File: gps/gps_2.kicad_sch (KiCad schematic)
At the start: 43 parts, among them J1 Programming Header, J2 G125-MH104M4-04AD000P, J3 SMA_CONN, U1 M10578-A2, U2 PIC18F26K83, U3 MCP2562, U4 SPX3819M5-L-3-3, U5 INA180

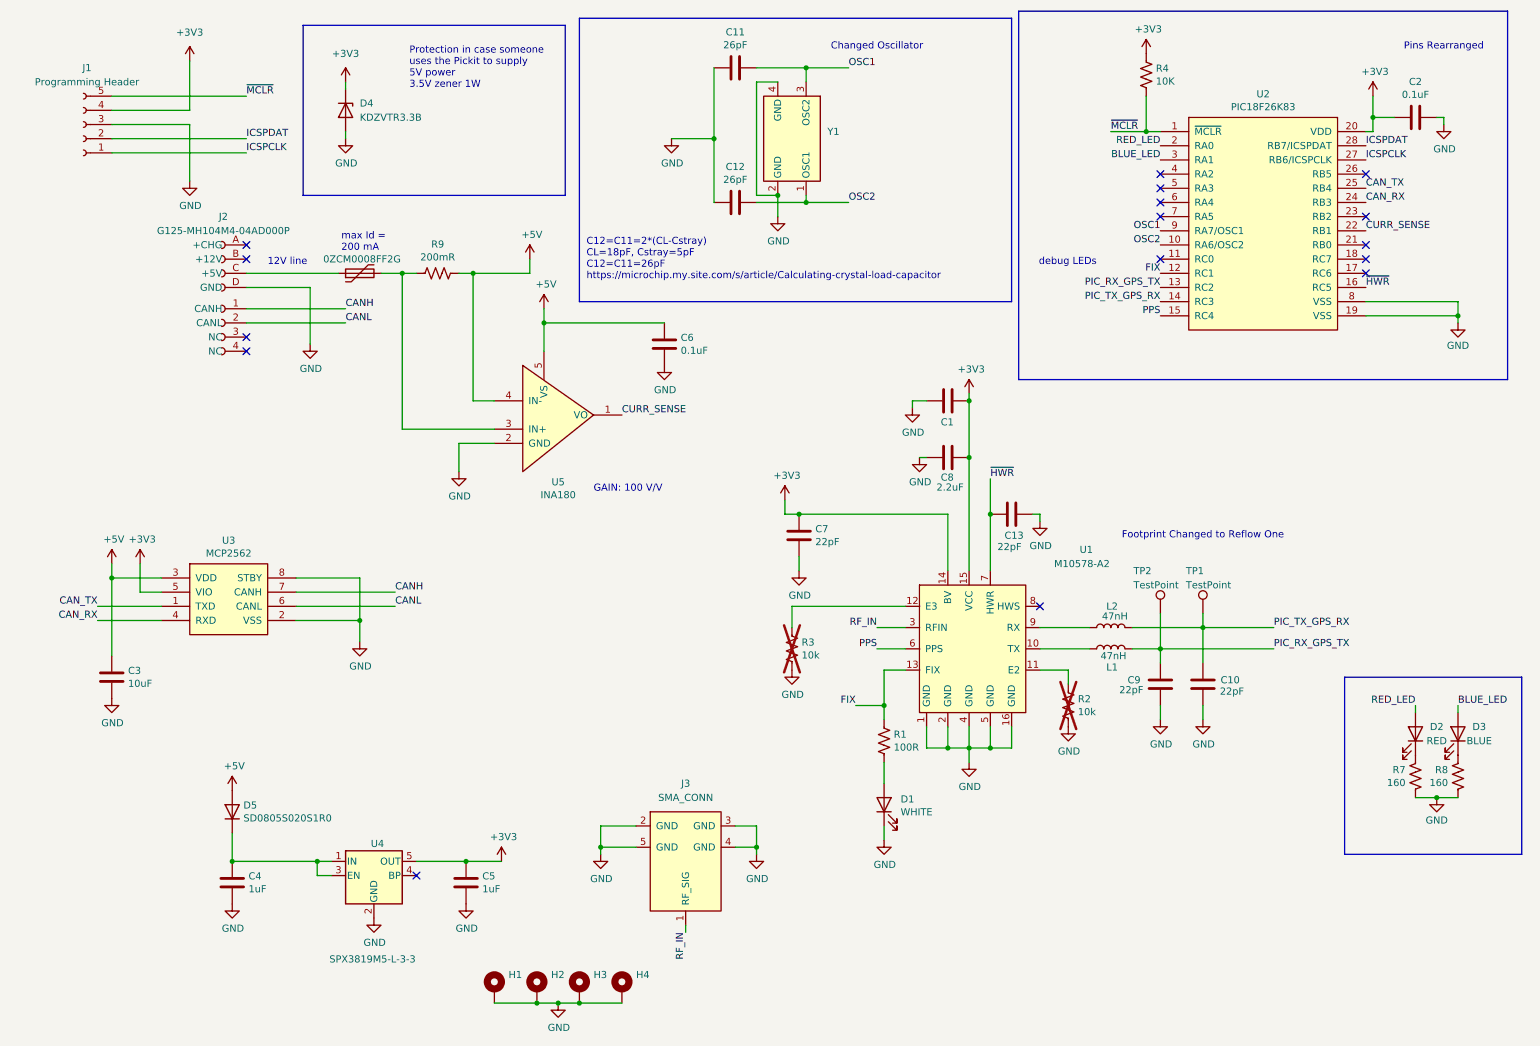
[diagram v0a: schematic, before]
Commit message: Added Rio's changes except TP's for CAN. Eliminated Diode from LDO input
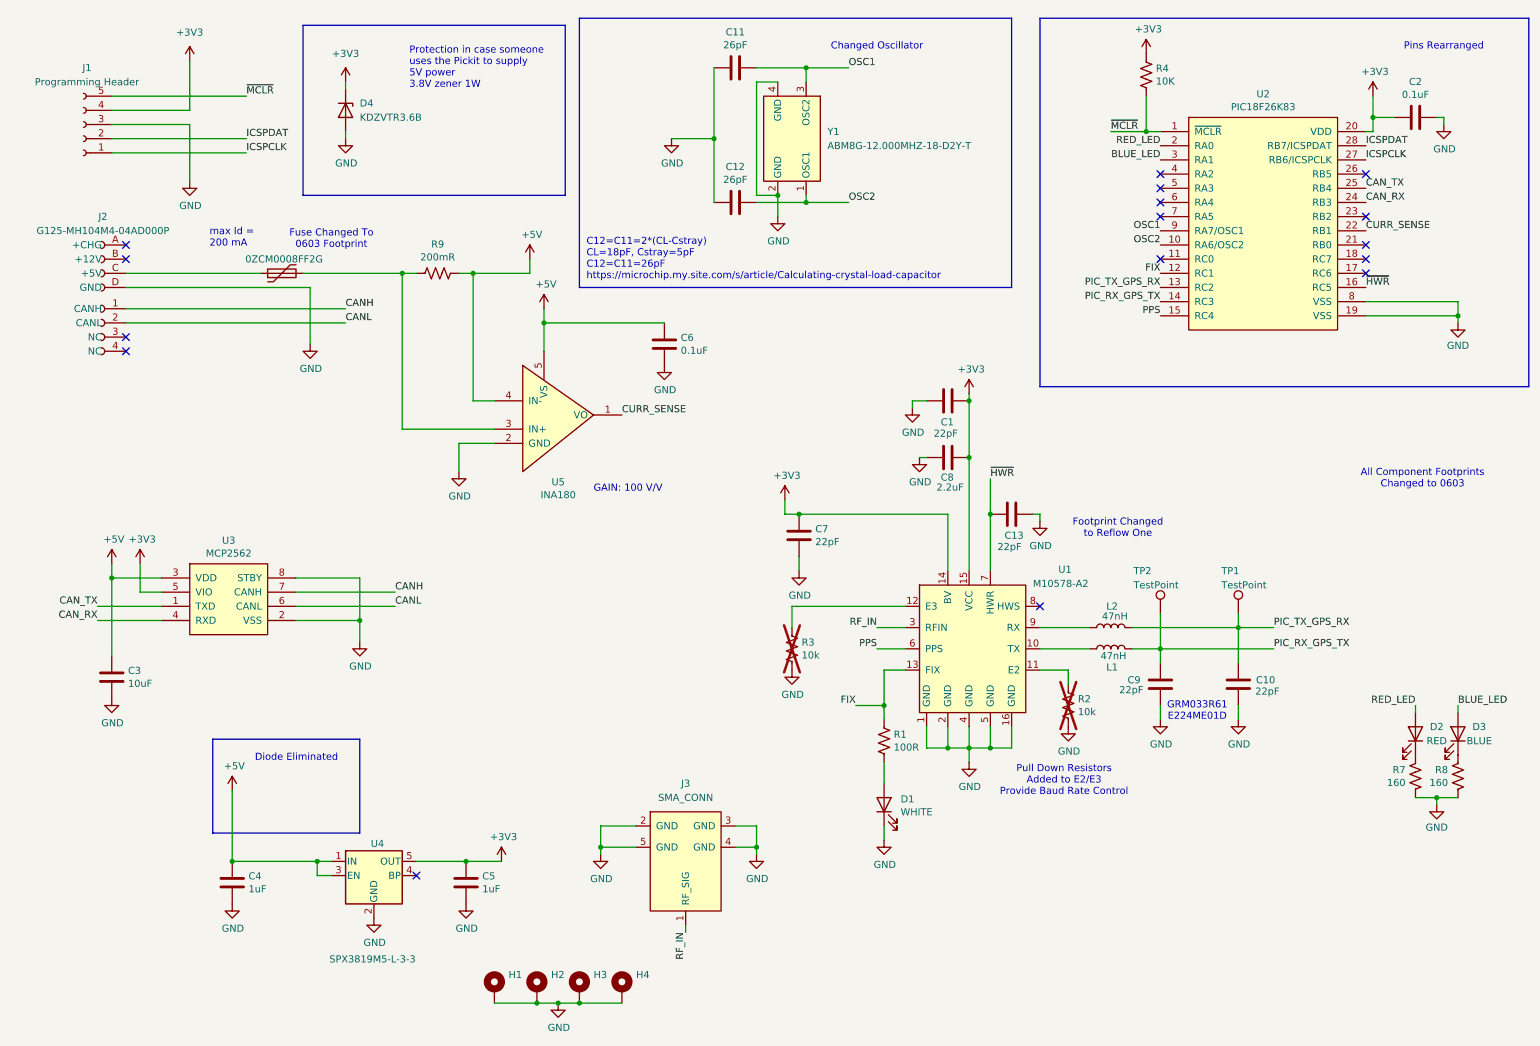
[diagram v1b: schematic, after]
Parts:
- removed D5: SD0805S020S1R0, SD0805S020S1R0:SD0805_AVX, symbol Device:D
- C11, C12: footprint Capacitor_SMD:C_0603_1608Metric_Pad1.08x0.95mm_HandSolder -> Capacitor_SMD:C_0805_2012Metric_Pad1.18x1.45mm_HandSolder
- D4: value KDZVTR3.3B -> KDZVTR3.6B
- Y1: value ~ -> ABM8G-12.000MHZ-18-D2Y-T
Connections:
- net +5V: now also C4.1, U4.1 (IN), U4.3 (EN)
- net PIC_RX_GPS_TX: now also U2.14 (RC3); no longer U2.13 (RC2)
- net PIC_TX_GPS_RX: now also U2.13 (RC2); no longer U2.14 (RC3)
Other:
- note added: "All Component Footprints Changed to 0603"
- note added: "Diode Eliminated"
- note added: "Fuse Changed To 0603 Footprint"
- note added: "GRM033R61 E224ME01D"
- note added: "Protection in case someone uses the Pickit to supply 5V power 3.8V zener 1W"
- note added: "Pull Down Resistors Added to E2/E3 Provide Baud Rate Control"
- note removed: "12V line"
- note removed: "Protection in case someone uses the Pickit to supply 5V power 3.5V zener 1W"
- note removed: "debug LEDs"
- moved on the sheet: C10, J2, TP1

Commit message: Final Ancilliary Changes
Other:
- note added: "Rough Documentation on Decisions"
- company: (none) -> Waterloo Rocketry
- title: (none) -> GPS Board
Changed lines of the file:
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@@
 	(generator_version "9.0")
 	(paper "A4")
+	(title_block
+		(title "GPS Board")
+		(date "2025-11-09")
+		(rev "AA")
+		(company "Waterloo Rocketry")
+		(comment 1 "Moved to new connector")
+	)
 	(rectangle
 		(start 48.5775 143.1925)
@@
 		)
 	)
+	(text "Rough Documentation on Decisions"
+		(exclude_from_sim no)
+		(at 230.124 164.084 0)
+		(effects
+			(font
+				(size 1.27 1.27)
+			)
+			(href "https://docs.google.com/document/d/1MVI2FVcVLvdXN6-vZZdgDN41M7ggt62CCTXvSoYcLLI/edit?tab=t.0")
+		)
+	)

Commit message: Added CANH/L and GND testpoints
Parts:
- added TP3: CANH, TestPoint:TestPoint_Keystone_5000-5004_Miniature, symbol Connector:TestPoint
- added TP4: CANL, TestPoint:TestPoint_Keystone_5000-5004_Miniature, symbol Connector:TestPoint
- added TP5: GND, TestPoint:TestPoint_Keystone_5000-5004_Miniature, symbol Connector:TestPoint
- TP1: value TestPoint -> RX
- TP2: value TestPoint -> TX
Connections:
- net CANH: now also TP3.1
- net CANL: now also TP4.1
- net GND: now also TP5.1

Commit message: Added Some Changes
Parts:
- TP3: value CANH -> 36-5001-ND
- TP4: value CANL -> 36-5001-ND
- TP5: value GND -> 36-5001-ND
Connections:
- net CANH: no longer TP3.1
- net CANL: no longer TP4.1
- net CAN_RX: now also TP4.1
- net CAN_TX: now also TP3.1
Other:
- moved on the sheet: C3, TP3, TP4, U3

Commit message: Moved CAN testpoints and removed GND Test point
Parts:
- removed TP5: 36-5001-ND, TestPoint:TestPoint_Keystone_5000-5004_Miniature, symbol Connector:TestPoint
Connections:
- net BLUE_LED: now also U2.11 (RC0); no longer U2.3 (RA1)
- net CAN_RX: now also U2.2 (RA0); no longer U2.24 (RB3)
- net CAN_TX: now also U2.3 (RA1); no longer U2.25 (RB4)
- net FIX: now also U2.7 (RA5); no longer U2.12 (RC1)
- net RED_LED: now also U2.12 (RC1); no longer U2.2 (RA0)
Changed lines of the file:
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@@
 	)
 	(no_connect
-		(at 218.44 49.53)
+		(at 255.27 46.99)
 	)
 	(no_connect
@@
 	)
 	(no_connect
-		(at 218.44 46.99)
+		(at 255.27 44.45)
 	)
 	(no_connect
-		(at 218.44 57.15)
+		(at 218.44 46.99)
 	)
 	(no_connect
@@
 	)
 	(label "CAN_TX"
-		(at 255.27 44.45 0)
+		(at 218.44 39.37 180)
 		(effects
 			(font
 				(size 1.27 1.27)
 			)
-			(justify left bottom)
+			(justify right bottom)
 		)
 	)
@@
 	)
 	(label "BLUE_LED"
-		(at 218.44 39.37 180)
+		(at 218.44 57.15 180)
 		(effects
 			(font
@@
 	)
 	(label "CAN_RX"
-		(at 255.27 46.99 0)
+		(at 218.44 36.83 180)
 		(effects
 			(font
 				(size 1.27 1.27)
 			)
-			(justify left bottom)
+			(justify right bottom)
 		)
 	)
@@
 	)
 	(label "RED_LED"
-		(at 218.44 36.83 180)
+		(at 218.44 59.69 180)
 		(effects
 			(font
@@
 	)
 	(label "FIX"
-		(at 218.44 59.69 180)
+		(at 218.44 49.53 180)
 		(effects
 			(font
@@
 	)
 	(symbol
-		(lib_id "power:GND")
-		(at 43.18 81.28 0)
-		(unit 1)
-		(exclude_from_sim no)
-		(in_bom yes)
-		(on_board yes)
-		(dnp no)
-		(property "Reference" "#PWR041"
-			(at 43.18 87.63 0)
-			(effects
-				(font
-					(size 1.27 1.27)
-				)
-				(hide yes)
-			)
-		)
-		(property "Value" "GND"
-			(at 43.307 85.6742 0)
-			(effects
-				(font
-					(size 1.27 1.27)
-				)
-			)
-		)
-		(property "Footprint" ""
-			(at 43.18 81.28 0)
-			(effects
-				(font
-					(size 1.27 1.27)
-				)
-				(hide yes)
-			)
-		)
-		(property "Datasheet" ""
-			(at 43.18 81.28 0)
-			(effects
-				(font
-					(size 1.27 1.27)
-				)
-				(hide yes)
-			)
-		)
-		(property "Description" "Power symbol creates a global label with name \"GND\" , ground"
-			(at 43.18 81.28 0)
-			(effects
-				(font
-					(size 1.27 1.27)
-				)
-				(hide yes)
-			)
-		)
-		(pin "1"
-		)
-		(instances
-			(project "gps_2"
-				(path "/997541fa-8f1b-4c61-890b-f0a276bced1e"
-					(reference "#PWR041")
-					(unit 1)
-				)
-			)
-		)
-	)
-	(symbol
 		(lib_id "canhw:G125-MH104M4-04AD000P")
 		(at 30.48 50.8 0)
@@
 					(unit 1)
 				)
-			)
-		)
-	)
-	(symbol
-		(lib_id "Connector:TestPoint")
-		(at 43.18 81.28 0)
-		(unit 1)
-		(exclude_from_sim no)
-		(in_bom yes)
-		(on_board yes)
-		(dnp no)
-		(fields_autoplaced yes)
-		(property "Reference" "TP5"
-			(at 45.72 76.7079 0)
-			(effects
-				(font
-					(size 1.27 1.27)
-				)
-				(justify left)
-			)
-		)
-		(property "Value" "36-5001-ND"
-			(at 45.72 79.2479 0)
-			(effects
-				(font
-					(size 1.27 1.27)
-				)
-				(justify left)
-			)
-		)
-		(property "Footprint" "TestPoint:TestPoint_Keystone_5000-5004_Miniature"
-			(at 48.26 81.28 0)
-			(effects
-				(font
-					(size 1.27 1.27)
-				)
-				(hide yes)
-			)
-		)
-		(property "Datasheet" "~"
-			(at 48.26 81.28 0)
-			(effects
-				(font
-					(size 1.27 1.27)
-				)
-				(hide yes)
-			)
-		)
-		(property "Description" "test point"
-			(at 43.18 81.28 0)
-			(effects
-				(font
-					(size 1.27 1.27)
-				)
-				(hide yes)
-			)
-		)
-		(pin "1"
-		)
-		(instances
-			(project ""
-				(path "/997541fa-8f1b-4c61-890b-f0a276bced1e"
-					(reference "TP5")
-					(unit 1)
-				)

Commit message: Added Edge Connector
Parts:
- removed J3: SMA_CONN, SMA_Conn:CONN_3-1478978-1_TEC, symbol canhw:SMA_CONN
- added J3: CON-SMA-EDGE-S, SMA_Edge:RFSOLUTIONS_CON-SMA-EDGE-S, symbol CON-SMA-EDGE-S:CON-SMA-EDGE-S
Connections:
- net GND: now also J3.G1, J3.G2, J3.G3, J3.G4
- net RF_IN: now also J3.1
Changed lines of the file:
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@@
 	)
 	(junction
-		(at 118.11 162.56)
-		(diameter 0)
-		(color 0 0 0 0)
-	)
-	(junction
 		(at 271.78 67.31)
 		(diameter 0)
@@
 	)
 	(junction
-		(at 146.05 162.56)
-		(diameter 0)
-		(color 0 0 0 0)
-	)
-	(junction
 		(at 138.43 35.56)
 		(diameter 0)
@@
 	(wire
 		(pts
-			(xy 133.35 176.53) (xy 133.35 177.8)
-		)
-		(stroke
-			(width 0)
-			(type default)
-		)
-	)
-	(wire
-		(pts
 			(xy 99.06 87.63) (xy 82.55 87.63)
 		)
@@
 	(wire
 		(pts
-			(xy 142.24 158.75) (xy 146.05 158.75)
-		)
-		(stroke
-			(width 0)
-			(type default)
-		)
-	)
-	(wire
-		(pts
 			(xy 213.36 127) (xy 218.44 127)
 		)
@@
 	(wire
 		(pts
-			(xy 146.05 163.83) (xy 146.05 162.56)
+			(xy 130.81 163.83) (xy 130.81 162.56)
 		)
 		(stroke
@@
 	(wire
 		(pts
-			(xy 146.05 158.75) (xy 146.05 162.56)
-		)
-		(stroke
-			(width 0)
-			(type default)
-		)
-	)
-	(wire
-		(pts
 			(xy 184.15 81.28) (xy 184.15 82.55)
 		)
@@
 	(wire
 		(pts
-			(xy 142.24 162.56) (xy 146.05 162.56)
+			(xy 127 162.56) (xy 130.81 162.56)
 		)
 		(stroke
@@
 	(wire
 		(pts
+			(xy 127 160.02) (xy 129.54 160.02)
+		)
+		(stroke
+			(width 0)
+			(type default)
+		)
+	)
+	(wire
+		(pts
 			(xy 33.02 119.38) (xy 24.13 119.38)
 		)
@@
 	(wire
 		(pts
-			(xy 124.46 158.75) (xy 118.11 158.75)
-		)
-		(stroke
-			(width 0)
-			(type default)
-		)
-	)
-	(wire
-		(pts
-			(xy 118.11 163.83) (xy 118.11 162.56)
-		)
-		(stroke
-			(width 0)
-			(type default)
-		)
-	)
-	(wire
-		(pts
 			(xy 114.3 190.5) (xy 121.92 190.5)
 		)
@@
 	(wire
 		(pts
-			(xy 124.46 162.56) (xy 118.11 162.56)
-		)
-		(stroke
-			(width 0)
-			(type default)
-		)
-	)
-	(wire
-		(pts
 			(xy 129.54 68.58) (xy 107.95 68.58)
 		)
@@
 		)
 	)
-	(wire
-		(pts
-			(xy 118.11 158.75) (xy 118.11 162.56)
-		)
-		(stroke
-			(width 0)
-			(type default)
-		)
-	)
 	(label "FIX"
 		(at 163.83 137.16 180)
@@
 	)
 	(label "RF_IN"
-		(at 133.35 177.8 270)
+		(at 129.54 160.02 0)
 		(effects
 			(font
 				(size 1.27 1.27)
 			)
-			(justify right bottom)
+			(justify left bottom)
 		)
 	)
@@
 	(symbol
 		(lib_id "power:GND")
-		(at 118.11 163.83 0)
-		(unit 1)
-		(exclude_from_sim no)
-		(in_bom yes)
-		(on_board yes)
-		(dnp no)
-		(property "Reference" "#PWR032"
-			(at 118.11 170.18 0)
-			(effects
-				(font
-					(size 1.27 1.27)
-				)
-				(hide yes)
-			)
-		)
-		(property "Value" "GND"
-			(at 118.237 168.2242 0)
-			(effects
-				(font
-					(size 1.27 1.27)
-				)
-			)
-		)
-		(property "Footprint" ""
-			(at 118.11 163.83 0)
-			(effects
-				(font
-					(size 1.27 1.27)
-				)
-				(hide yes)
-			)
-		)
-		(property "Datasheet" ""
-			(at 118.11 163.83 0)
-			(effects
-				(font
-					(size 1.27 1.27)
-				)
-				(hide yes)
-			)
-		)
-		(property "Description" "Power symbol creates a global label with name \"GND\" , ground"
-			(at 118.11 163.83 0)
-			(effects
-				(font
-					(size 1.27 1.27)
-				)
-				(hide yes)
-			)
-		)
-		(pin "1"
-		)
-		(instances
-			(project ""
-				(path "/997541fa-8f1b-4c61-890b-f0a276bced1e"
-					(reference "#PWR032")
-					(unit 1)
-				)
-			)
-		)
-	)
-	(symbol
-		(lib_id "power:GND")
 		(at 168.91 161.29 0)
 		(unit 1)
@@
 	(symbol
 		(lib_id "power:GND")
-		(at 146.05 163.83 0)
+		(at 130.81 163.83 0)
 		(unit 1)
 		(exclude_from_sim no)
@@
 		(dnp no)
 		(property "Reference" "#PWR033"
-			(at 146.05 170.18 0)
+			(at 130.81 170.18 0)
 			(effects
 				(font
@@
 		)
 		(property "Value" "GND"
-			(at 146.177 168.2242 0)
+			(at 130.937 168.2242 0)
 			(effects
 				(font
@@
 		)
 		(property "Footprint" ""
-			(at 146.05 163.83 0)
+			(at 130.81 163.83 0)
 			(effects
 				(font
@@
 		)
 		(property "Datasheet" ""
-			(at 146.05 163.83 0)
+			(at 130.81 163.83 0)
 			(effects
 				(font
@@
 		)
 		(property "Description" "Power symbol creates a global label with name \"GND\" , ground"
-			(at 146.05 163.83 0)
+			(at 130.81 163.83 0)
 			(effects
 				(font
@@
 	)
 	(symbol
+		(lib_id "CON-SMA-EDGE-S:CON-SMA-EDGE-S")
+		(at 124.46 162.56 0)
+		(unit 1)
+		(exclude_from_sim no)
+		(in_bom yes)
+		(on_board yes)
+		(dnp no)
+		(fields_autoplaced yes)
+		(property "Reference" "J3"
+			(at 124.079 153.67 0)
+			(effects
+				(font
+					(size 1.27 1.27)
+				)
+			)
+		)
+		(property "Value" "CON-SMA-EDGE-S"
+			(at 124.079 156.21 0)
+			(effects
+				(font
+					(size 1.27 1.27)
+				)
+			)
+		)
+		(property "Footprint" "SMA_Edge:RFSOLUTIONS_CON-SMA-EDGE-S"
+			(at 124.46 162.56 0)
+			(effects
+				(font
+					(size 1.27 1.27)
+				)
+				(justify bottom)
+				(hide yes)
+			)
+		)
+		(property "Datasheet" ""
+			(at 124.46 162.56 0)
+			(effects
+				(font
+					(size 1.27 1.27)
+				)
+				(hide yes)
+			)
+		)
+		(property "Description" ""
+			(at 124.46 162.56 0)
+			(effects
+				(font
+					(size 1.27 1.27)
+				)
+				(hide yes)
+			)
+		)
+		(property "PARTREV" "1"
+			(at 124.46 162.56 0)
+			(effects
+				(font
+					(size 1.27 1.27)
+				)
+				(justify bottom)
+				(hide yes)
+			)
+		)
+		(property "STANDARD" "Manufacturer Recommendations"
+			(at 124.46 162.56 0)
+			(effects
+				(font
+					(size 1.27 1.27)
+				)
+				(justify bottom)
+				(hide yes)
+			)
+		)
+		(property "MAXIMUM_PACKAGE_HEIGHT" "6.35mm"
+			(at 124.46 162.56 0)
+			(effects
+				(font
+					(size 1.27 1.27)
+				)
+				(justify bottom)
+				(hide yes)
+			)
+		)
+		(property "MANUFACTURER" "RF Solutions"
+			(at 124.46 162.56 0)
+			(effects
+				(font
+					(size 1.27 1.27)
+				)
+				(justify bottom)
+				(hide yes)
+			)
+		)
+		(pin "G1"
+		)
+		(pin "G2"
+		)
+		(pin "G4"
+		)
+		(pin "G3"
+		)
+		(pin "1"
+		)
+		(instances
+			(project ""
+				(path "/997541fa-8f1b-4c61-890b-f0a276bced1e"
+					(reference "J3")
+					(unit 1)
+				)
+			)
+		)
+	)
+	(symbol
 		(lib_id "Mechanical:MountingHole_Pad")
 		(at 106.68 187.96 0)
@@
 					(unit 1)
 				)
-			)
-		)
-	)
-	(symbol
-		(lib_id "canhw:SMA_CONN")
-		(at 133.35 165.1 0)
-		(unit 1)
-		(exclude_from_sim no)
-		(in_bom yes)
-		(on_board yes)
-		(dnp no)
-		(fields_autoplaced yes)
-		(property "Reference" "J3"
-			(at 133.35 151.13 0)
-			(effects
-				(font
-					(size 1.27 1.27)
-				)
-			)
-		)
-		(property "Value" "SMA_CONN"
-			(at 133.35 153.67 0)
-			(effects
-				(font
-					(size 1.27 1.27)
-				)
-			)
-		)
-		(property "Footprint" "SMA_Conn:CONN_3-1478978-1_TEC"
-			(at 132.08 161.29 0)
-			(effects
-				(font
-					(size 1.27 1.27)
-				)
-				(hide yes)
-			)
-		)
-		(property "Datasheet" "https://www.te.com/usa-en/product-3-1478978-1.datasheet.pdf"
-			(at 132.08 161.29 0)
-			(effects
-				(font
-					(size 1.27 1.27)
-				)
-				(hide yes)
-			)
-		)
-		(property "Description" ""
-			(at 133.35 165.1 0)
-			(effects
-				(font
-					(size 1.27 1.27)
-				)
-				(hide yes)
-			)
-		)
-		(pin "1"
-		)
-		(pin "2"
-		)
-		(pin "5"
-		)
-		(pin "3"
-		)
-		(pin "4"
-		)
-		(instances
-			(project ""
-				(path "/997541fa-8f1b-4c61-890b-f0a276bced1e"
-					(reference "J3")
-					(unit 1)
-				)

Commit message: Changed to same edge connector as LTT and made kicad-footprints a submodule
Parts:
- removed J3: CON-SMA-EDGE-S, SMA_Edge:RFSOLUTIONS_CON-SMA-EDGE-S, symbol CON-SMA-EDGE-S:CON-SMA-EDGE-S
- added J3: EMPCB.SMAFSTJ.B.HT, EMPCB_SMAFSTJ_B_HT:TAOGLAS_EMPCB.SMAFSTJ.B.HT, symbol EMPCB.SMAFSTJ.B.HT:EMPCB.SMAFSTJ.B.HT
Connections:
- net GND: now also J3.SH1, J3.SH2, J3.SH3, J3.SH4
- net RF_IN: now also J3.1

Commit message: Fixed CAN Pins, and kelvin sense connection
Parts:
- removed H1, H2, H3, H4: MountingHole_Pad, MountingHole:MountingHole_3.2mm_M3_DIN965_Pad_TopBottom, symbol Mechanical:MountingHole_Pad
- added H1, H2, H3, H4: MountingHole, MountingHole:MountingHole_3.2mm_M3, symbol Mechanical:MountingHole
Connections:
- net CAN_RX: now also U2.25 (RB4); no longer U2.2 (RA0)
- net CAN_TX: now also U2.26 (RB5); no longer U2.3 (RA1)
